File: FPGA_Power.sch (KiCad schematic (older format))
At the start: 2 parts

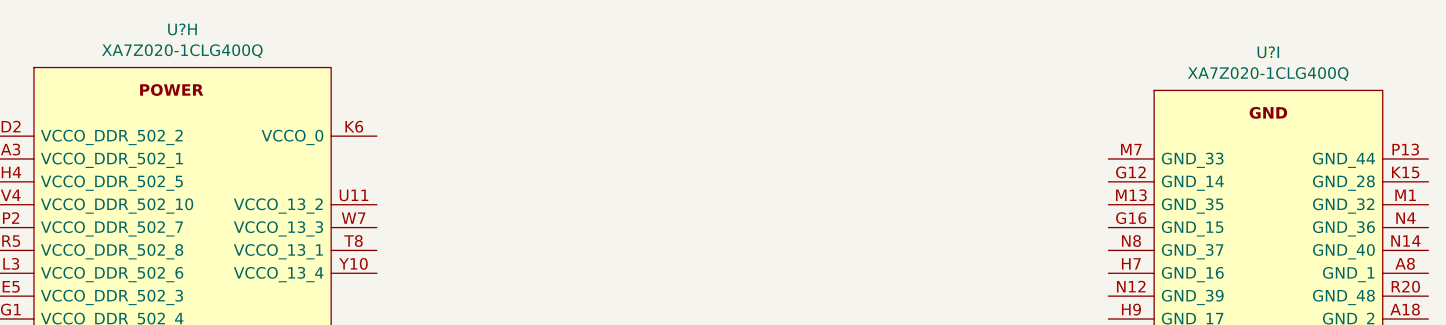
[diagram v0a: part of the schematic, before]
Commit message: Completeed the FPGA_Power sheet Created PCB
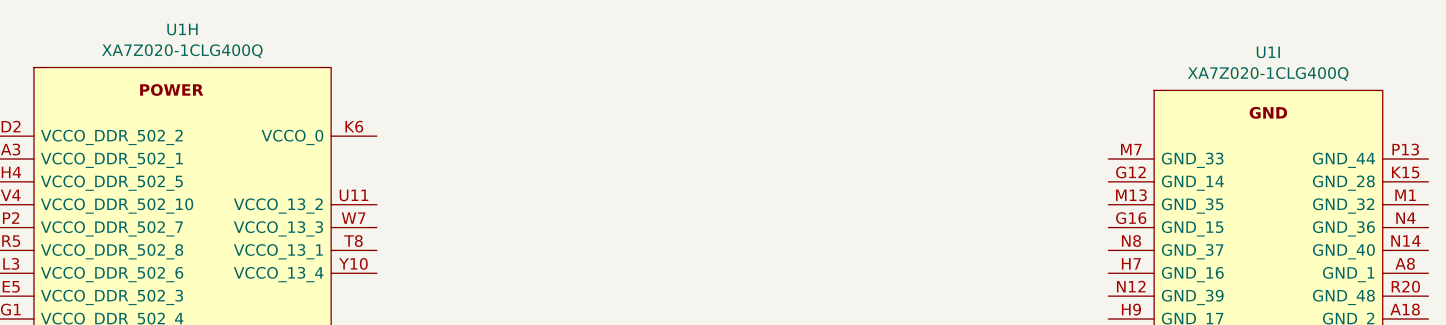
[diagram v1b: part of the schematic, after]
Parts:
- gave numbers to parts that had none: 1
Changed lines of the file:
@@
 $EndDescr
 $Comp
-L GM_FPGA:XA7Z020-1CLG400Q U?
+L GM_FPGA:XA7Z020-1CLG400Q U1
 U 8 1 6019CD0B
 P 2900 1100
-F 0 "U?" H 3550 1265 50  0000 C CNN
+F 0 "U1" H 3550 1265 50  0000 C CNN
 F 1 "XA7Z020-1CLG400Q" H 3550 1174 50  0000 C CNN
 F 2 "BGA400C80P20X20_1700X1700X160" H 5750 1200 50  0001 L CNN
@@
 $EndComp
 $Comp
-L GM_FPGA:XA7Z020-1CLG400Q U?
+L GM_FPGA:XA7Z020-1CLG400Q U1
 U 9 1 601D4472
 P 7800 1200
-F 0 "U?" H 8300 1365 50  0000 C CNN
+F 0 "U1" H 8300 1365 50  0000 C CNN
 F 1 "XA7Z020-1CLG400Q" H 8300 1274 50  0000 C CNN
 F 2 "BGA400C80P20X20_1700X1700X160" H 10650 1300 50  0001 L CNN
